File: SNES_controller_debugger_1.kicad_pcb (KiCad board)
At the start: 2 copper layers, 100 x 74 mm, 28 parts, among them J1 ICSP, J2 CONTROLLER_OUT, J3 MICRO_USB, Q1 DMG2302UK-7, Q2 DMP2215L-7, SW1 Reset_switch, U1 ATmega32U4, Y1 16MHz

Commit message: pcb: Tweak LCD screen footprint and a few traces
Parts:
- moved SW1 5.15 mm to (134.9, 155.7), turned to 180 degrees
- moved DS1 0.46 mm to (90.0, 89.5)
- moved R8 0.20 mm to (92.2, 144.2)
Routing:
- net VCC: track 215.9 -> 224.6 mm
- net Net-(DS1-Pad2): track 89.8 -> 86.6 mm, vias 0 -> 2

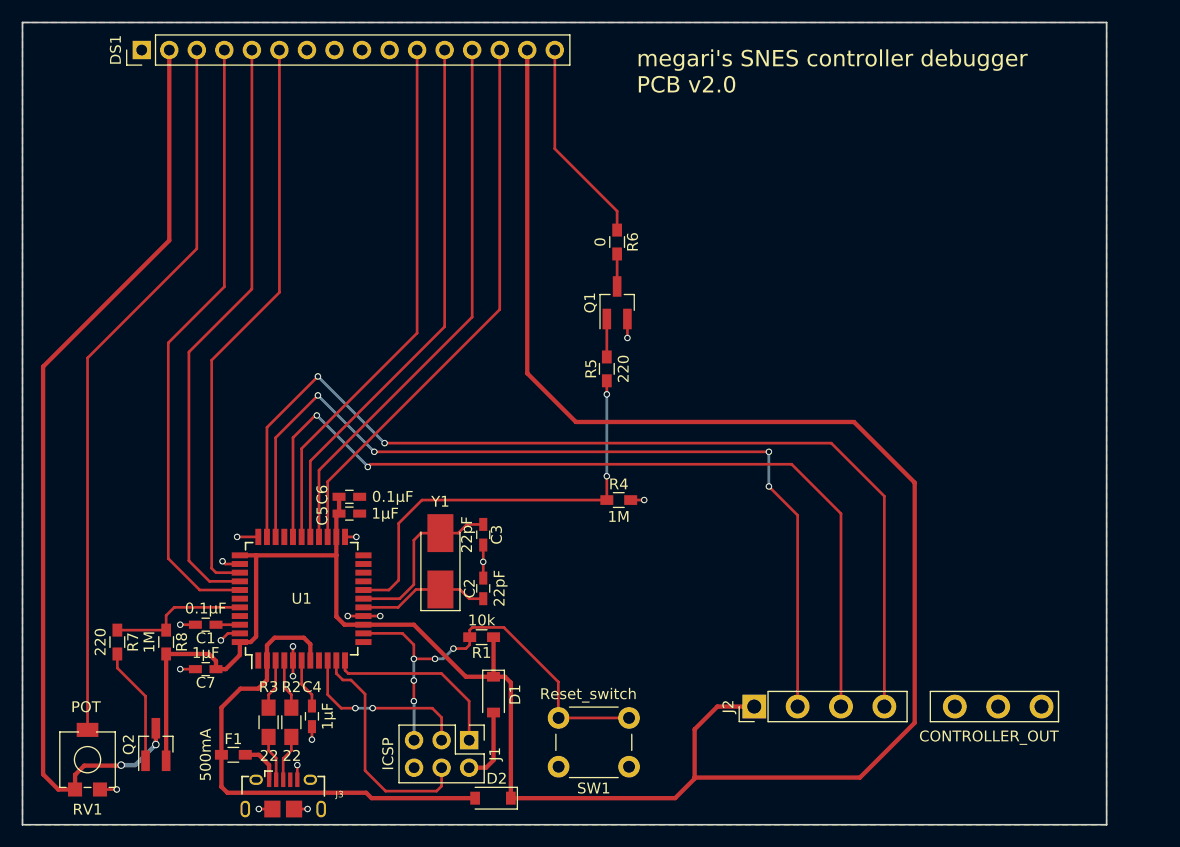
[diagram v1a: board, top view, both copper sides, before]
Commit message: pcb: Add holes corresponding to where they are on the LCD, tweak some silkscreen texts
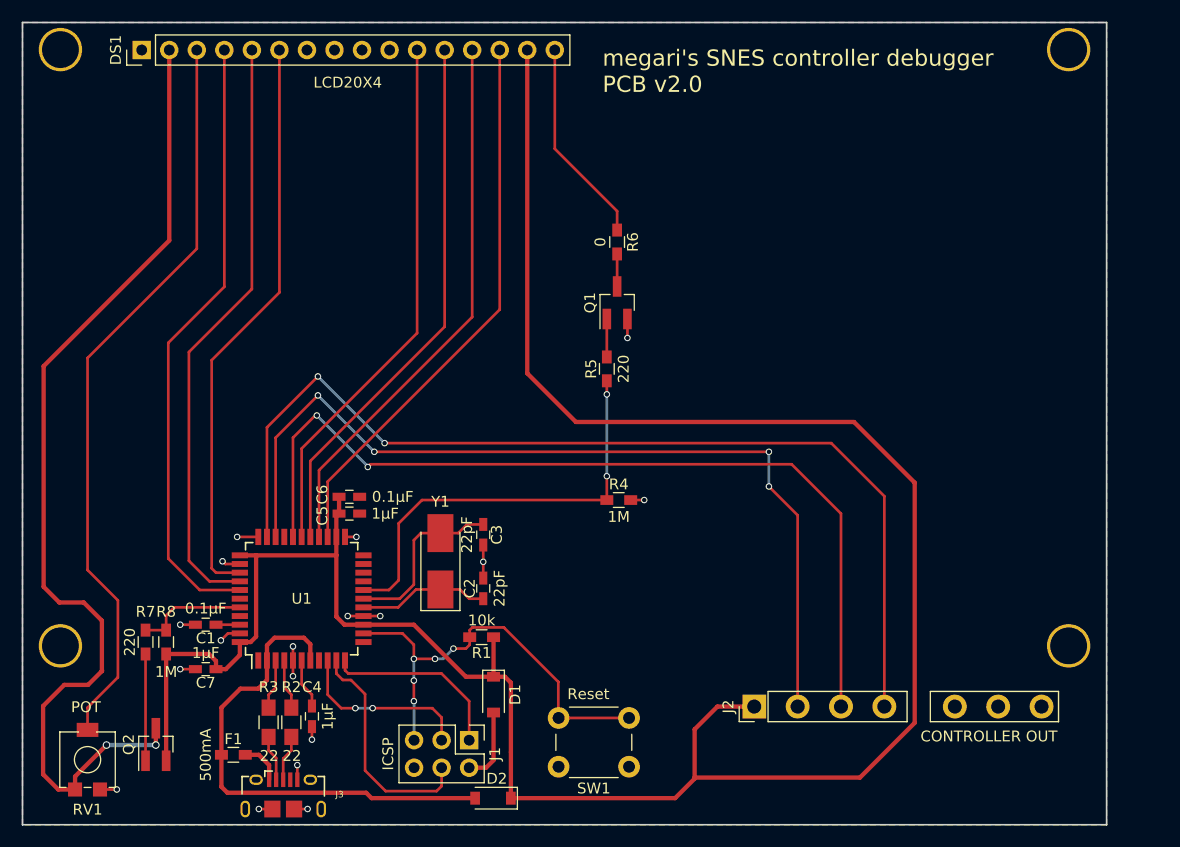
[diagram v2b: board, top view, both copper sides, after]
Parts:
- added H1: MountingHole_3.4mm, Megaris_fixed_footprints:MountingHole_3.4mm, F.Cu at (82.5, 89.5)
- added H2: MountingHole_3.4mm, Megaris_fixed_footprints:MountingHole_3.4mm, F.Cu at (175.5, 89.5)
- added H3: MountingHole_3.4mm, Megaris_fixed_footprints:MountingHole_3.4mm, F.Cu at (82.5, 144.5)
- added H4: MountingHole_3.4mm, Megaris_fixed_footprints:MountingHole_3.4mm, F.Cu at (175.5, 144.5)
- J2: value CONTROLLER_OUT -> CONTROLLER OUT
- SW1: value Reset_switch -> Reset
- moved R7 2.60 mm to (90.3, 144.2)
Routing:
- net Net-(DS1-Pad2): track 86.6 -> 93.7 mm
- net LCD_PWR: track 13.0 -> 10.4 mm
- net Net-(DS1-Pad3): track 66.9 -> 69.2 mm
- net Net-(Q2-Pad1): track 10.9 -> 9.85 mm
